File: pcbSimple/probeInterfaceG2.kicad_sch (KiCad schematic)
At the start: 20 parts, among them J1 Conn_01x20_Female, J2 Conn_01x20_Female, J3 Conn_02x05_Odd_Even, J4 Conn_01x20_Female, J5 Conn_01x20_Female, U1 SN74AVC4T774GUX

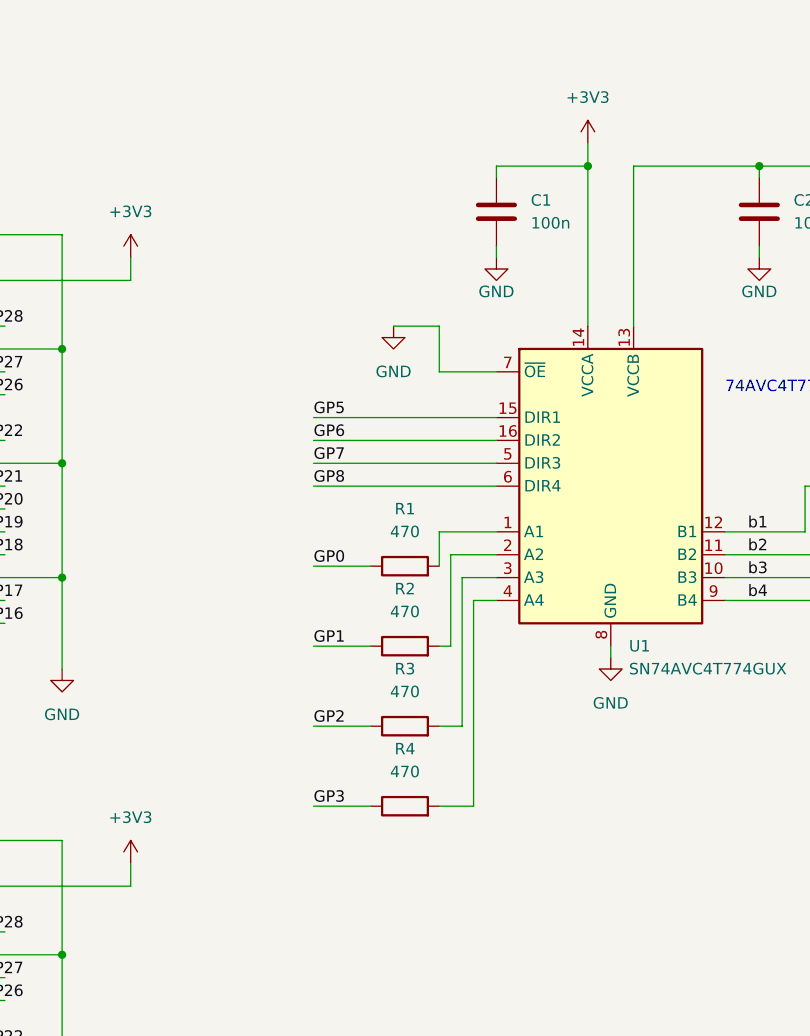
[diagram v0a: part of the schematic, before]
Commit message: simplified simplePCB
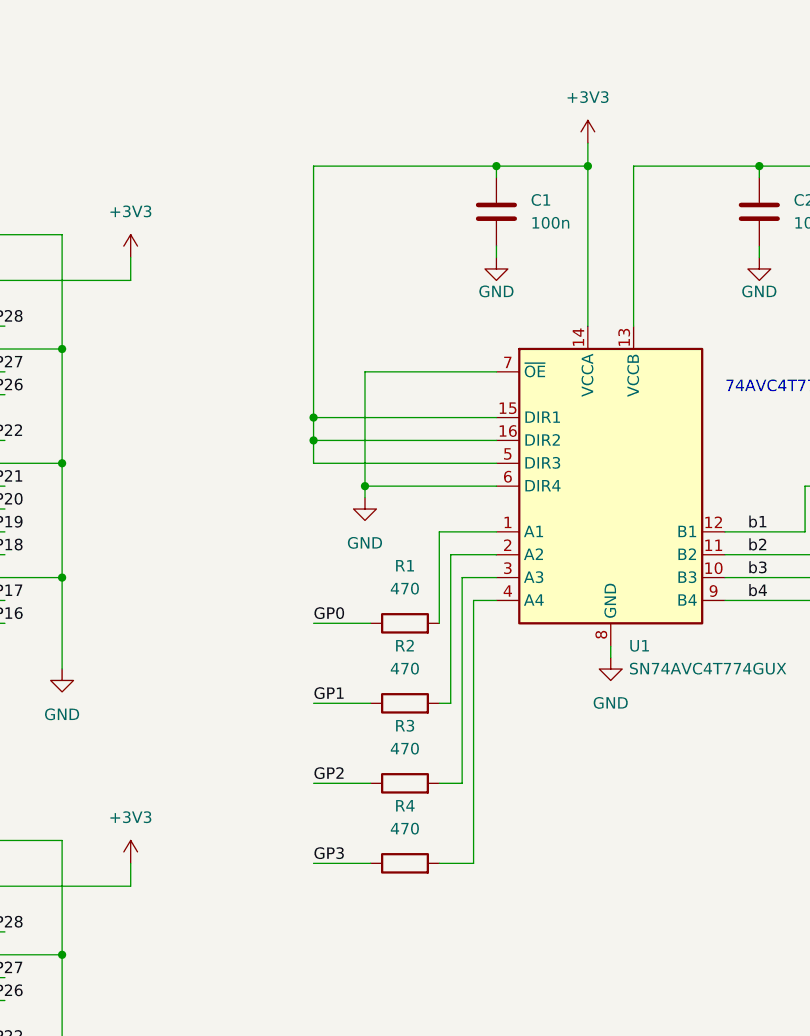
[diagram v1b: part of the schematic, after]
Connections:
- net +3V3: now also U1.15 (DIR1), U1.16 (DIR2), U1.5 (DIR3)
- net GND: now also U1.6 (DIR4)
- net GP5: no longer U1.15 (DIR1)
- net GP6: no longer U1.16 (DIR2)
- net GP7: no longer U1.5 (DIR3)
- net GP8: no longer U1.6 (DIR4)
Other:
- moved on the sheet: R1, R2, R3, R4
